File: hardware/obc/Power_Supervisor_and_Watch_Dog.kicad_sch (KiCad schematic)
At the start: 23 parts, among them J201 Conn_01x02, Q51 IRF7306, Q52 PMBT2222A, Q53 MBT2222ADW1T1, Q54 MBT2222ADW1T1

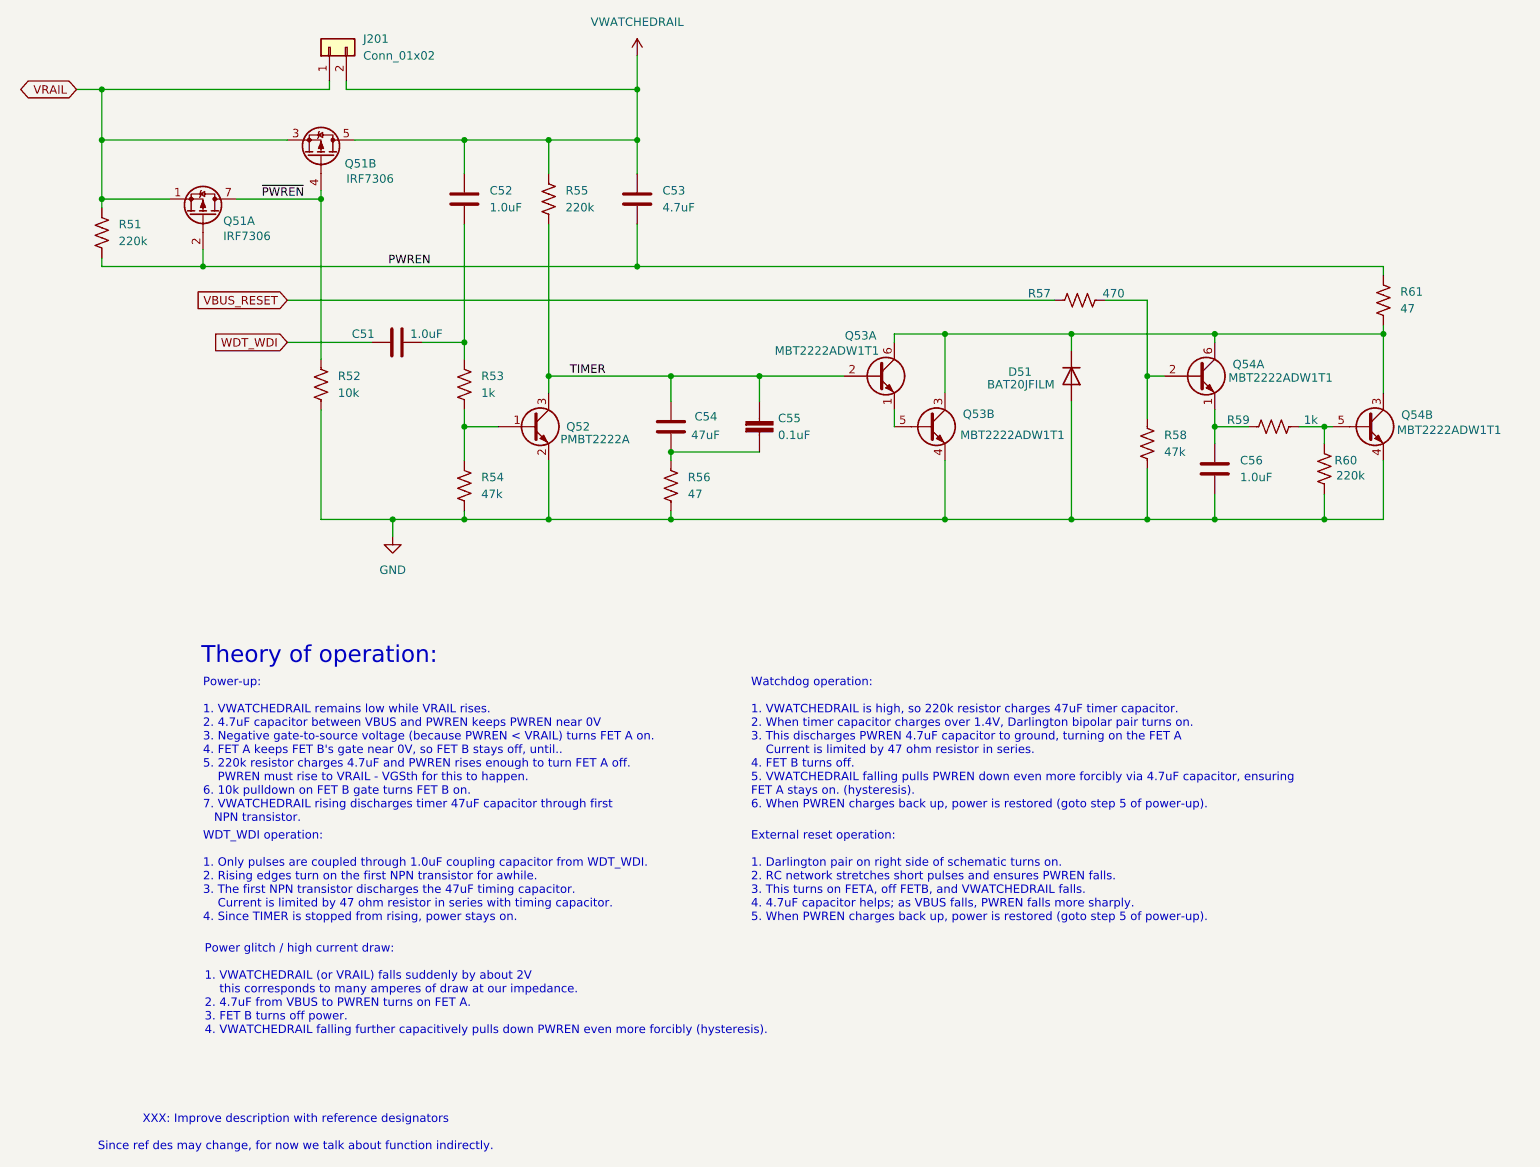
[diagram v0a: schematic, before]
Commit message: obc: BOM and schematic cleanup
- remove unused fields
- remove incorrect datasheets
- fix a connector 'value' field (CONx02 instead of x05)
- add documentation to power supervisor page

This is in preparation for a comprehensive review pass by me.

In the layout, some issues were identified (QSPI_* pins routed
suboptimally, silkscreen on pads, and some layer reduction could
take place.  Bouncing this back to Luke for further work before
my review pass there.
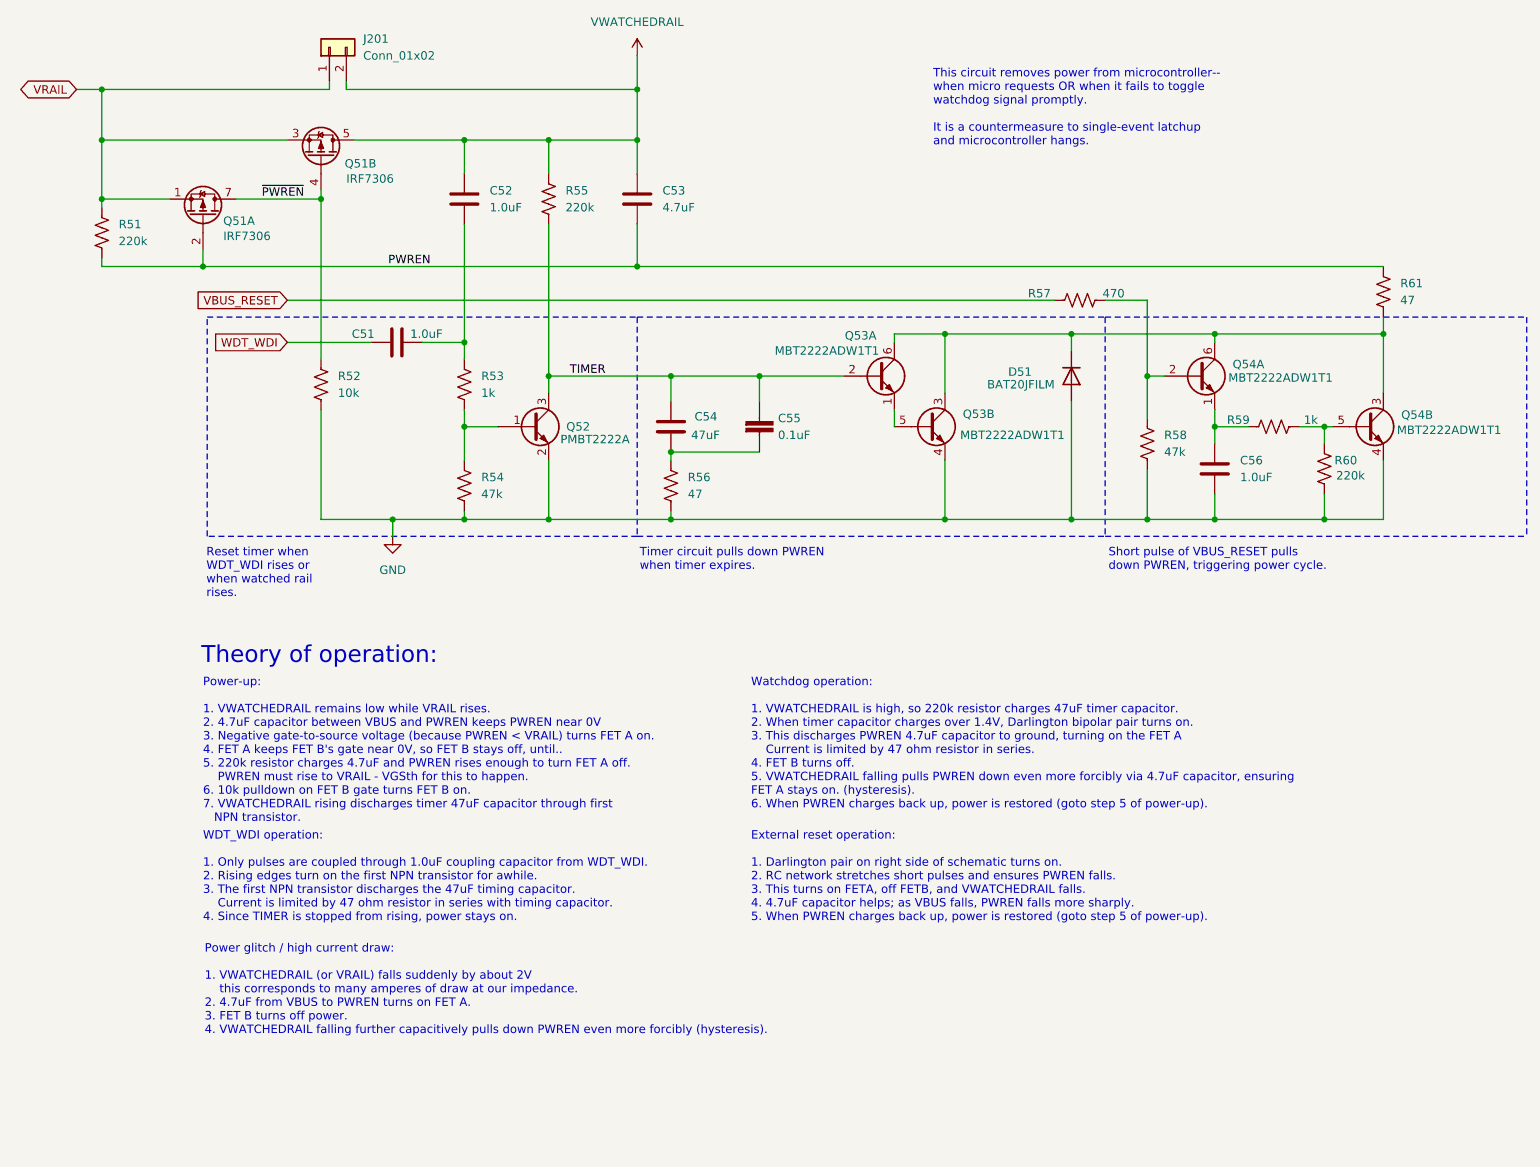
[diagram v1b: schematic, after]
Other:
- note added: "Reset timer when WDT_WDI rises or when watched rail rises."
- note added: "Short pulse of VBUS_RESET pulls down PWREN, triggering power cycle."
- note added: "This circuit removes power from microcontroller-- when micro requests OR when it fails to toggle watchdog signal promptly. It is a countermeasure to single-event latchup and microcontroller hangs."
- note added: "Timer circuit pulls down PWREN when timer expires."
- note removed: "XXX: Improve description with reference designators Since ref des may change, for now we talk about function indirectly."
- moved on the sheet: R61
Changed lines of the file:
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@@
 		)
 	)
+	(polyline
+		(pts
+			(xy 109.855 93.98) (xy 180.34 93.98)
+		)
+		(stroke
+			(width 0)
+			(type dash)
+		)
+	)
+	(polyline
+		(pts
+			(xy 180.34 60.96) (xy 180.34 93.98)
+		)
+		(stroke
+			(width 0)
+			(type dash)
+		)
+	)
 	(wire
 		(pts
@@
 		)
 	)
+	(polyline
+		(pts
+			(xy 109.855 60.96) (xy 180.34 60.96)
+		)
+		(stroke
+			(width 0)
+			(type dash)
+		)
+	)
 	(wire
 		(pts
@@
 	(wire
 		(pts
-			(xy 222.25 62.23) (xy 222.25 63.5)
+			(xy 222.25 60.96) (xy 222.25 63.5)
 		)
 		(stroke
@@
 	(wire
 		(pts
-			(xy 222.25 53.34) (xy 222.25 54.61)
+			(xy 222.25 63.5) (xy 222.25 72.39)
 		)
 		(stroke
@@
 	(wire
 		(pts
-			(xy 222.25 63.5) (xy 222.25 72.39)
+			(xy 213.36 77.47) (xy 214.63 77.47)
 		)
 		(stroke
@@
 		)
 	)
-	(wire
+	(polyline
 		(pts
-			(xy 213.36 77.47) (xy 214.63 77.47)
+			(xy 243.84 60.96) (xy 243.84 93.98)
 		)
 		(stroke
 			(width 0)
-			(type default)
+			(type dash)
 		)
 	)
@@
 		)
 	)
+	(polyline
+		(pts
+			(xy 180.34 60.96) (xy 243.84 60.96)
+		)
+		(stroke
+			(width 0)
+			(type dash)
+		)
+	)
 	(wire
 		(pts
@@
 		)
 	)
+	(polyline
+		(pts
+			(xy 180.34 93.98) (xy 243.84 93.98)
+		)
+		(stroke
+			(width 0)
+			(type dash)
+		)
+	)
 	(wire
 		(pts
@@
 		)
 	)
+	(rectangle
+		(start 45.085 60.96)
+		(end 109.855 93.98)
+		(stroke
+			(width 0)
+			(type dash)
+		)
+		(fill
+			(type none)
+		)
+	)
 	(text "External reset operation:\n\n1. Darlington pair on right side of schematic turns on.\n2. RC network stretches short pulses and ensures PWREN falls.\n3. This turns on FETA, off FETB, and VWATCHEDRAIL falls.\n4. 4.7uF capacitor helps; as VBUS falls, PWREN falls more sharply.\n5. When PWREN charges back up, power is restored (goto step 5 of power-up)."
 		(exclude_from_sim no)
@@
 		)
 	)
-	(text "XXX: Improve description with reference designators\n\nSince ref des may change, for now we talk about function indirectly."
+	(text "Timer circuit pulls down PWREN\nwhen timer expires."
 		(exclude_from_sim no)
-		(at 58.42 183.896 0)
+		(at 110.236 95.758 0)
 		(effects
 			(font
 				(size 1.27 1.27)
 			)
+			(justify left top)
 		)
 	)
@@
 		)
 	)
+	(text "This circuit removes power from microcontroller--\nwhen micro requests OR when it fails to toggle\nwatchdog signal promptly.\n\nIt is a countermeasure to single-event latchup\nand microcontroller hangs."
+		(exclude_from_sim no)
+		(at 154.432 23.622 0)
+		(effects
+			(font
+				(size 1.27 1.27)
+			)
+			(justify left top)
+		)
+	)
+	(text "Short pulse of VBUS_RESET pulls \ndown PWREN, triggering power cycle."
+		(exclude_from_sim no)
+		(at 180.848 95.758 0)
+		(effects
+			(font
+				(size 1.27 1.27)
+			)
+			(justify left top)
+		)
+	)
 	(text "Power-up:\n\n1. VWATCHEDRAIL remains low while VRAIL rises.\n2. 4.7uF capacitor between VBUS and PWREN keeps PWREN near 0V\n3. Negative gate-to-source voltage (because PWREN < VRAIL) turns FET A on.\n4. FET A keeps FET B's gate near 0V, so FET B stays off, until..\n5. 220k resistor charges 4.7uF and PWREN rises enough to turn FET A off.\n	PWREN must rise to VRAIL - VGSth for this to happen.\n6. 10k pulldown on FET B gate turns FET B on.\n7. VWATCHEDRAIL rising discharges timer 47uF capacitor through first\n   NPN transistor."
 		(exclude_from_sim no)
@@
 		)
 	)
+	(text "Reset timer when\nWDT_WDI rises or\nwhen watched rail\nrises."
+		(exclude_from_sim no)
+		(at 44.958 95.758 0)
+		(effects
+			(font
+				(size 1.27 1.27)
+			)
+			(justify left top)
+		)
+	)
 	(text "Theory of operation:"
 		(exclude_from_sim no)
@@
 			)
 		)
-		(property "Datasheet" "~"
+		(property "Datasheet" ""
 			(at 73.66 64.77 0)
 			(effects
@@
 			)
 		)
-		(property "Datasheet" "~"
+		(property "Datasheet" ""
 			(at 83.82 43.18 0)
 			(effects
@@
 			)
 		)
-		(property "Datasheet" "~"
+		(property "Datasheet" ""
 			(at 196.85 83.82 0)
 			(effects
@@
 			)
 		)
-		(property "Datasheet" "~"
+		(property "Datasheet" ""
 			(at 29.21 48.26 0)
 			(effects
@@
 			)
 		)
-		(property "Datasheet" "~"
+		(property "Datasheet" ""
 			(at 114.935 86.36 0)
 			(effects
@@
 			)
 		)
-		(property "Datasheet" "~"
+		(property "Datasheet" ""
 			(at 175.26 69.85 0)
 			(effects
@@
 			)
 		)
-		(property "Datasheet" "~"
+		(property "Datasheet" ""
 			(at 96.52 43.18 0)
 			(effects
@@
 			)
 		)
-		(property "Datasheet" "~"
+		(property "Datasheet" ""
 			(at 176.53 58.42 0)
 			(effects
@@
 			)
 		)
-		(property "Datasheet" "~"
+		(property "Datasheet" ""
 			(at 186.69 80.01 0)
 			(effects
@@
 			)
 		)
-		(property "Datasheet" "~"
+		(property "Datasheet" ""
 			(at 63.5 20.32 0)
 			(effects
@@
 	(symbol
 		(lib_id "Device:R_US")
-		(at 222.25 58.42 0)
+		(at 222.25 57.15 0)
 		(unit 1)
 		(exclude_from_sim no)
@@
 		(dnp no)
 		(property "Reference" "R61"
-			(at 224.79 57.1499 0)
+			(at 224.79 55.8799 0)
 			(effects
 				(font
@@
 		)
 		(property "Value" "47"
-			(at 224.79 59.6899 0)
+			(at 224.79 58.4199 0)
 			(effects
 				(font
@@
 		)
 		(property "Footprint" "Resistor_SMD:R_0603_1608Metric"
-			(at 223.266 58.674 90)
+			(at 223.266 57.404 90)
 			(effects
 				(font
@@
 			)
 		)
-		(property "Datasheet" "~"
-			(at 222.25 58.42 0)
+		(property "Datasheet" ""
+			(at 222.25 57.15 0)
 			(effects
 				(font
@@
 		)
 		(property "Description" "Resistor, US symbol"
-			(at 222.25 58.42 0)
+			(at 222.25 57.15 0)
 			(effects
 				(font
@@
 		)
 		(property "LCSC" "C114623"
-			(at 222.25 58.42 0)
+			(at 222.25 57.15 0)
 			(effects
 				(font
@@
 		)
 		(property "Sim.Type" ""
-			(at 222.25 58.42 0)
+			(at 222.25 57.15 0)
 			(effects
 				(font
@@
 			)
 		)
-		(property "Datasheet" "~"
+		(property "Datasheet" ""
 			(at 114.935 77.47 0)
 			(effects
@@
 			)
 		)
-		(property "Datasheet" "~"
+		(property "Datasheet" ""
 			(at 83.82 86.36 0)
 			(effects
@@
 			)
 		)
-		(property "Datasheet" "~"
+		(property "Datasheet" ""
 			(at 213.36 83.82 0)
 			(effects

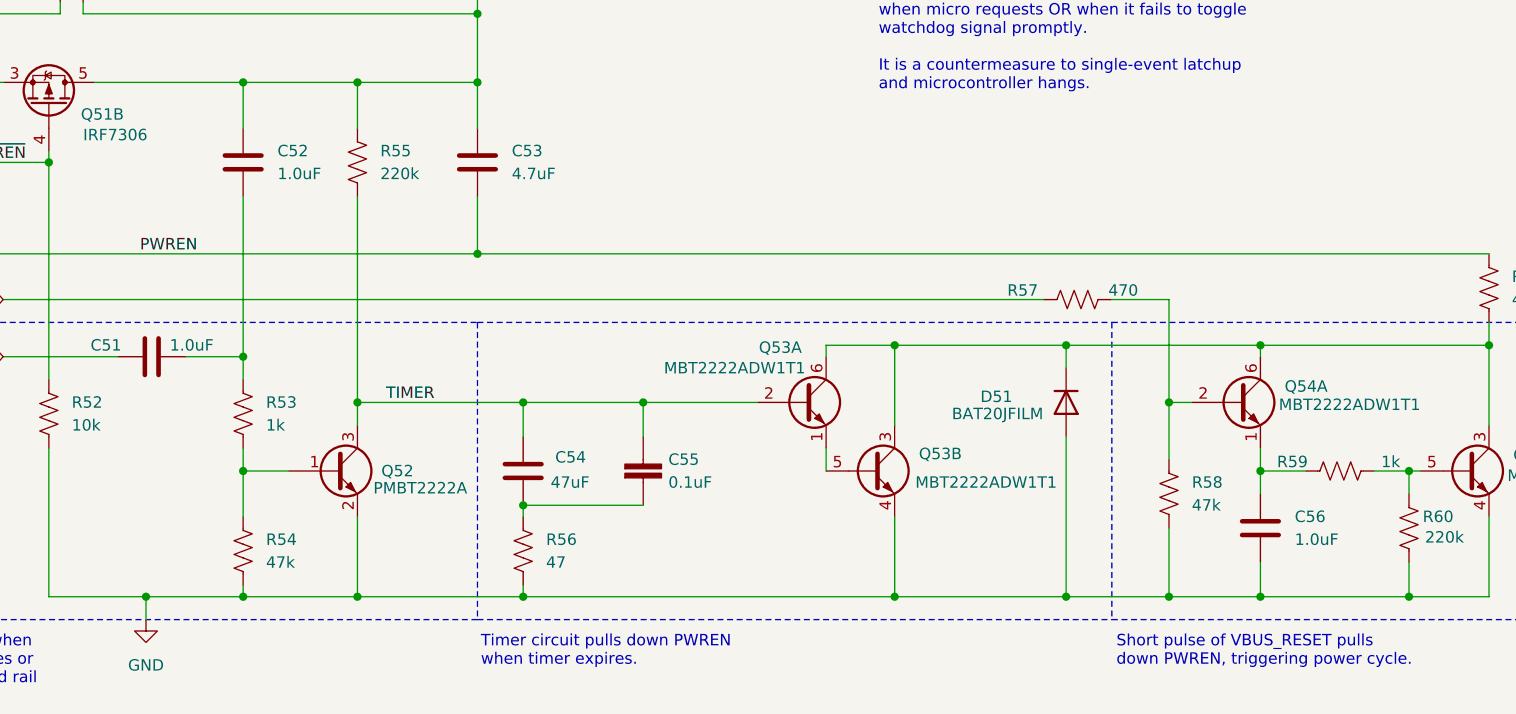
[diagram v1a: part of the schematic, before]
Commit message: obc: cleaned up BOM and re-routed MRAM and PSRAM
- cleaned up notes that no longer applied and changed some LCSC part numbers
- Gave QSPI_CLK a better route
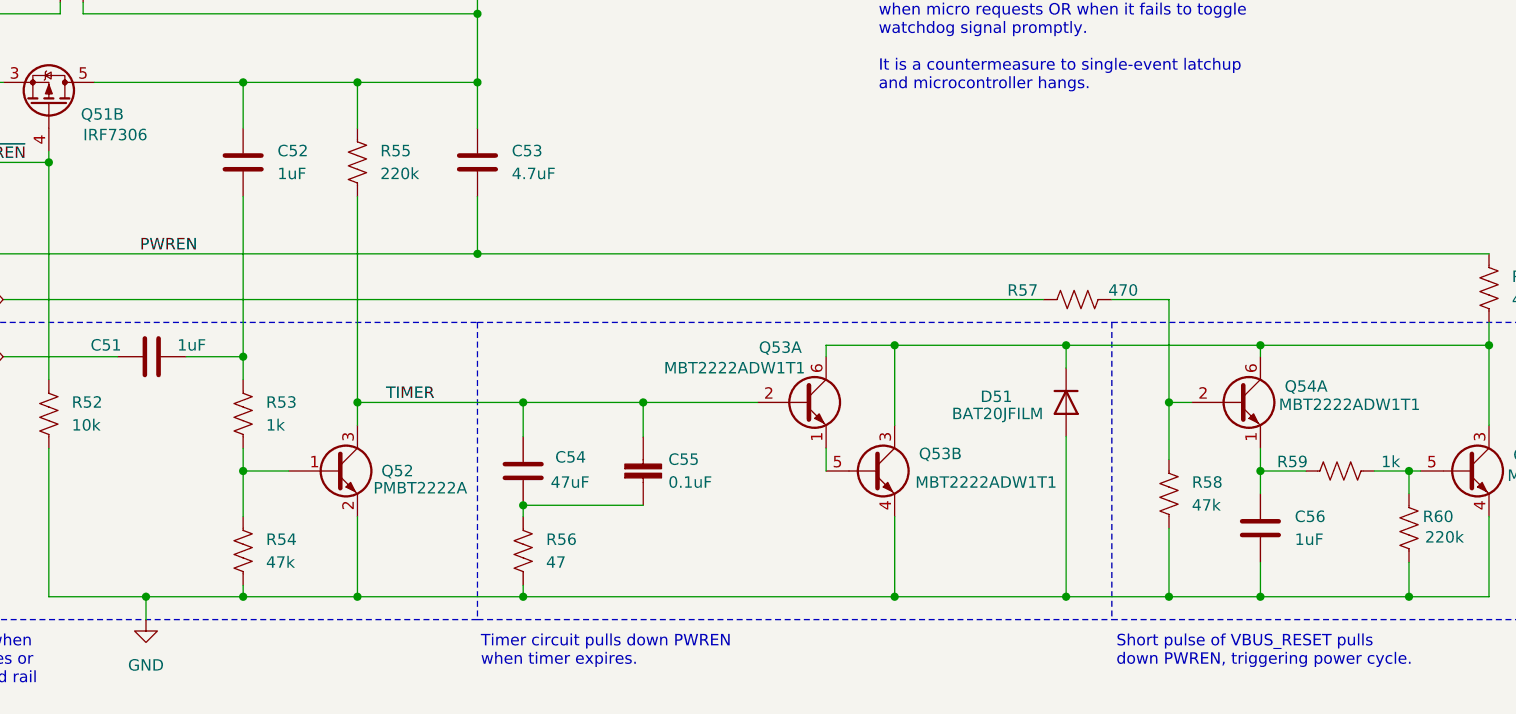
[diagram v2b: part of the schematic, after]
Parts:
- C51, C52, C56: value 1.0uF -> 1uF; Manufacturer_Name (none) -> Samsung Electro-Mechanics; Manufacturer_Part_Number (none) -> CL10B105KO8NNNC
- C54: footprint Capacitor_SMD:C_0603_1608Metric -> Capacitor_SMD:C_0805_2012Metric; LCSC C94034 -> C124129; Manufacturer_Name (none) -> Murata
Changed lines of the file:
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@@
 			)
 		)
-		(property "Value" "1.0uF"
+		(property "Value" "1uF"
 			(at 78.105 63.5 90)
 			(effects
@@
 			)
 		)
-		(property "Description" "Unpolarized capacitor"
+		(property "Description" "16V 1uF X7R ±10% 0603"
 			(at 73.66 64.77 0)
 			(effects
@@
 		)
 		(property "Sim.Type" ""
+			(at 73.66 64.77 0)
+			(effects
+				(font
+					(size 1.27 1.27)
+				)
+				(hide yes)
+			)
+		)
+		(property "Manufacturer_Name" " Samsung Electro-Mechanics"
+			(at 73.66 64.77 0)
+			(effects
+				(font
+					(size 1.27 1.27)
+				)
+				(hide yes)
+			)
+		)
+		(property "Manufacturer_Part_Number" " CL10B105KO8NNNC"
 			(at 73.66 64.77 0)
 			(effects
@@
 			)
 		)
-		(property "Value" "1.0uF"
+		(property "Value" "1uF"
 			(at 87.63 44.4499 0)
 			(effects
@@
 			)
 		)
-		(property "Description" "Unpolarized capacitor"
+		(property "Description" "16V 1uF X7R ±10% 0603"
 			(at 83.82 43.18 0)
 			(effects
@@
 		)
 		(property "Sim.Type" ""
+			(at 83.82 43.18 0)
+			(effects
+				(font
+					(size 1.27 1.27)
+				)
+				(hide yes)
+			)
+		)
+		(property "Manufacturer_Name" " Samsung Electro-Mechanics"
+			(at 83.82 43.18 0)
+			(effects
+				(font
+					(size 1.27 1.27)
+				)
+				(hide yes)
+			)
+		)
+		(property "Manufacturer_Part_Number" " CL10B105KO8NNNC"
 			(at 83.82 43.18 0)
 			(effects
@@
 			)
 		)
-		(property "Value" "1.0uF"
+		(property "Value" "1uF"
 			(at 200.66 85.0899 0)
 			(effects
@@
 			)
 		)
-		(property "Description" "Unpolarized capacitor"
+		(property "Description" "16V 1uF X7R ±10% 0603"
 			(at 196.85 83.82 0)
 			(effects
@@
 		)
 		(property "Sim.Type" ""
+			(at 196.85 83.82 0)
+			(effects
+				(font
+					(size 1.27 1.27)
+				)
+				(hide yes)
+			)
+		)
+		(property "Manufacturer_Name" " Samsung Electro-Mechanics"
+			(at 196.85 83.82 0)
+			(effects
+				(font
+					(size 1.27 1.27)
+				)
+				(hide yes)
+			)
+		)
+		(property "Manufacturer_Part_Number" " CL10B105KO8NNNC"
 			(at 196.85 83.82 0)
 			(effects
@@
 			)
 		)
-		(property "Footprint" "Capacitor_SMD:C_0603_1608Metric"
+		(property "Footprint" "Capacitor_SMD:C_0805_2012Metric"
 			(at 113.9698 73.66 0)
 			(effects
@@
 			)
 		)
-		(property "Description" "Unpolarized capacitor"
+		(property "Description" ""
 			(at 114.935 77.47 0)
 			(effects
@@
 			)
 		)
-		(property "LCSC" "C94034"
+		(property "LCSC" "C124129"
 			(at 114.935 77.47 0)
 			(effects
@@
 			(at 114.935 77.47 0)
 			(effects
+				(font
+					(size 1.27 1.27)
+				)
+				(hide yes)
+			)
+		)
+		(property "Manufacturer_Name" "Murata"
+			(at 114.935 77.47 0)
+			(effects

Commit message: ob: revised BOM and cleaned up PCB traces
- fixed BOM issues noticed
- added 2 extra capacitors on vwatchedrail and near 3.3v regulator
- cleaned up traces and did layer reduction
- moved whole watchdog circuit to a better location so all components can be close together
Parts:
- C53: LCSC C1705 -> C19666; Manufacturer_Part_Number CL10A475KP8NNNC -> CL10A475KO8NNNC
- R52: LCSC C169849 -> C191124
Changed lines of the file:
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@@
 			)
 		)
-		(property "LCSC" "C169849"
+		(property "LCSC" "C191124"
 			(at 62.23 71.12 0)
 			(effects
@@
 			)
 		)
-		(property "Description" "10V 4.7uF X5R ±10% 0603"
+		(property "Description" "16V 4.7uF X5R ±10% 0603"
 			(at 109.855 43.18 0)
 			(effects
@@
 			)
 		)
-		(property "LCSC" "C1705"
+		(property "LCSC" " C19666"
 			(at 109.855 43.18 0)
 			(effects
@@
 			)
 		)
-		(property "Manufacturer_Part_Number" "CL10A475KP8NNNC"
+		(property "Manufacturer_Part_Number" "CL10A475KO8NNNC"
 			(at 109.855 43.18 0)
 			(effects
